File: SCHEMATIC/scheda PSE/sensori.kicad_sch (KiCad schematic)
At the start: 17 parts, among them J5 I2C_3V3, J6 UART0_3V3, Q3 IRLML9301, U7 SAM-M8Q, U8 MMA8451Q, U9 TC1047A

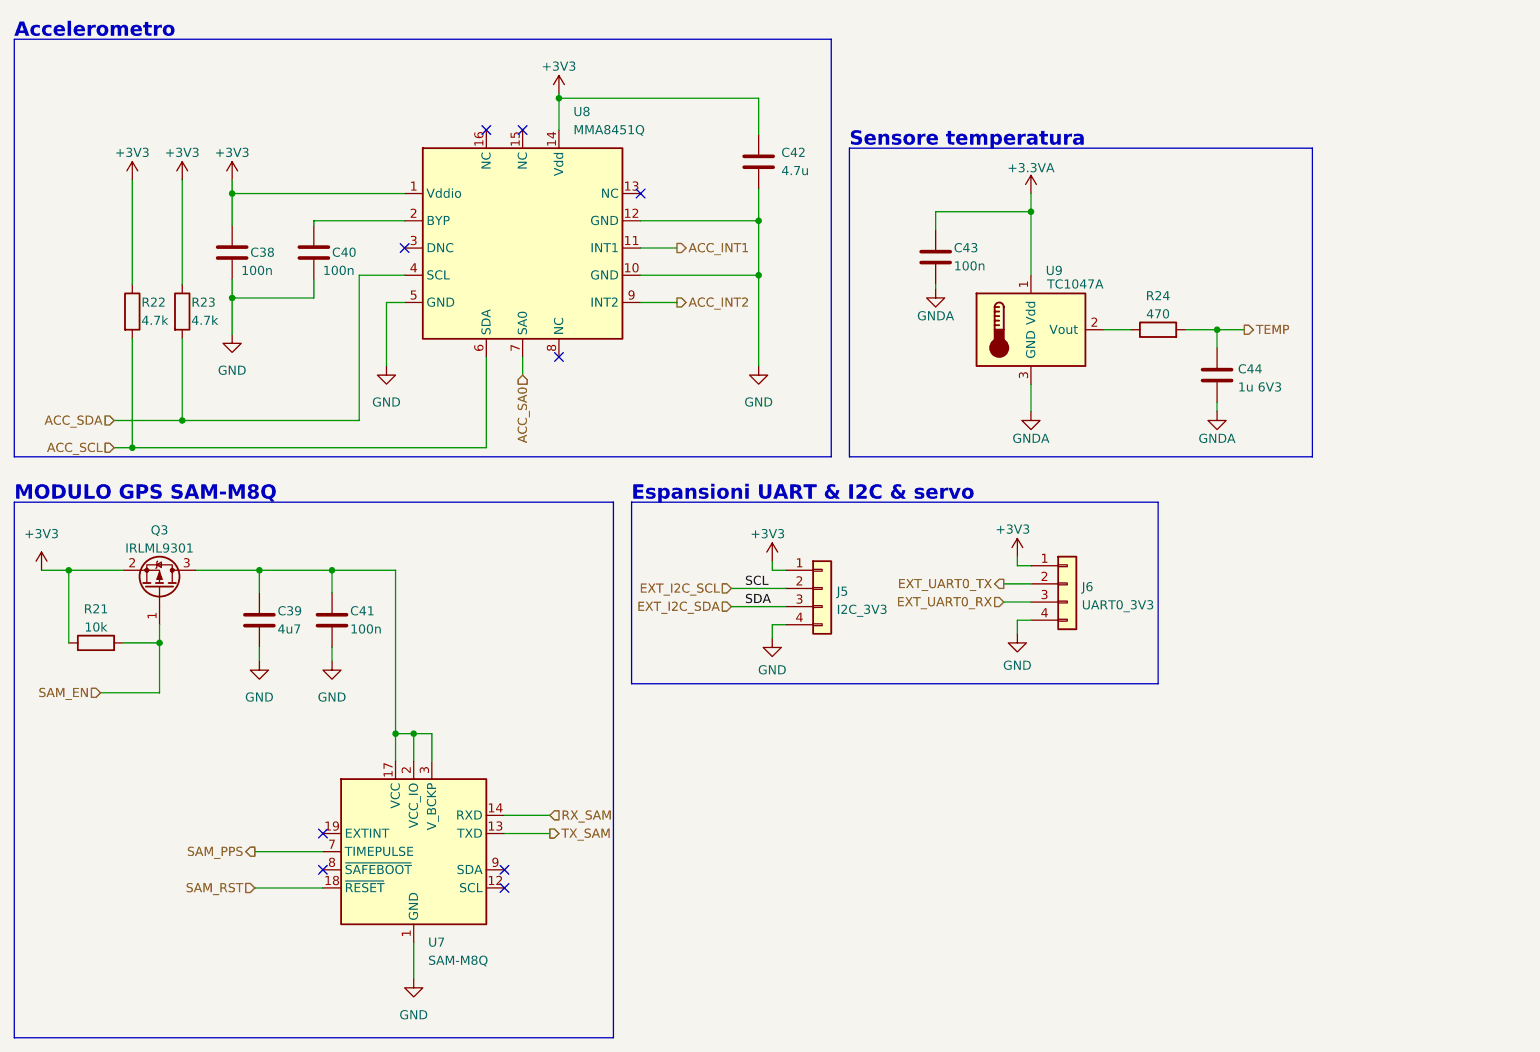
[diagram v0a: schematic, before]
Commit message: Aggiunte tutte le cose richieste dal prof
Aggiunte tutte le cose richieste dal prof:
wifi
servo
uscita led
MANCA DA METERE IL SOLDER MASK SUI PAD NON USATI DEL GPS
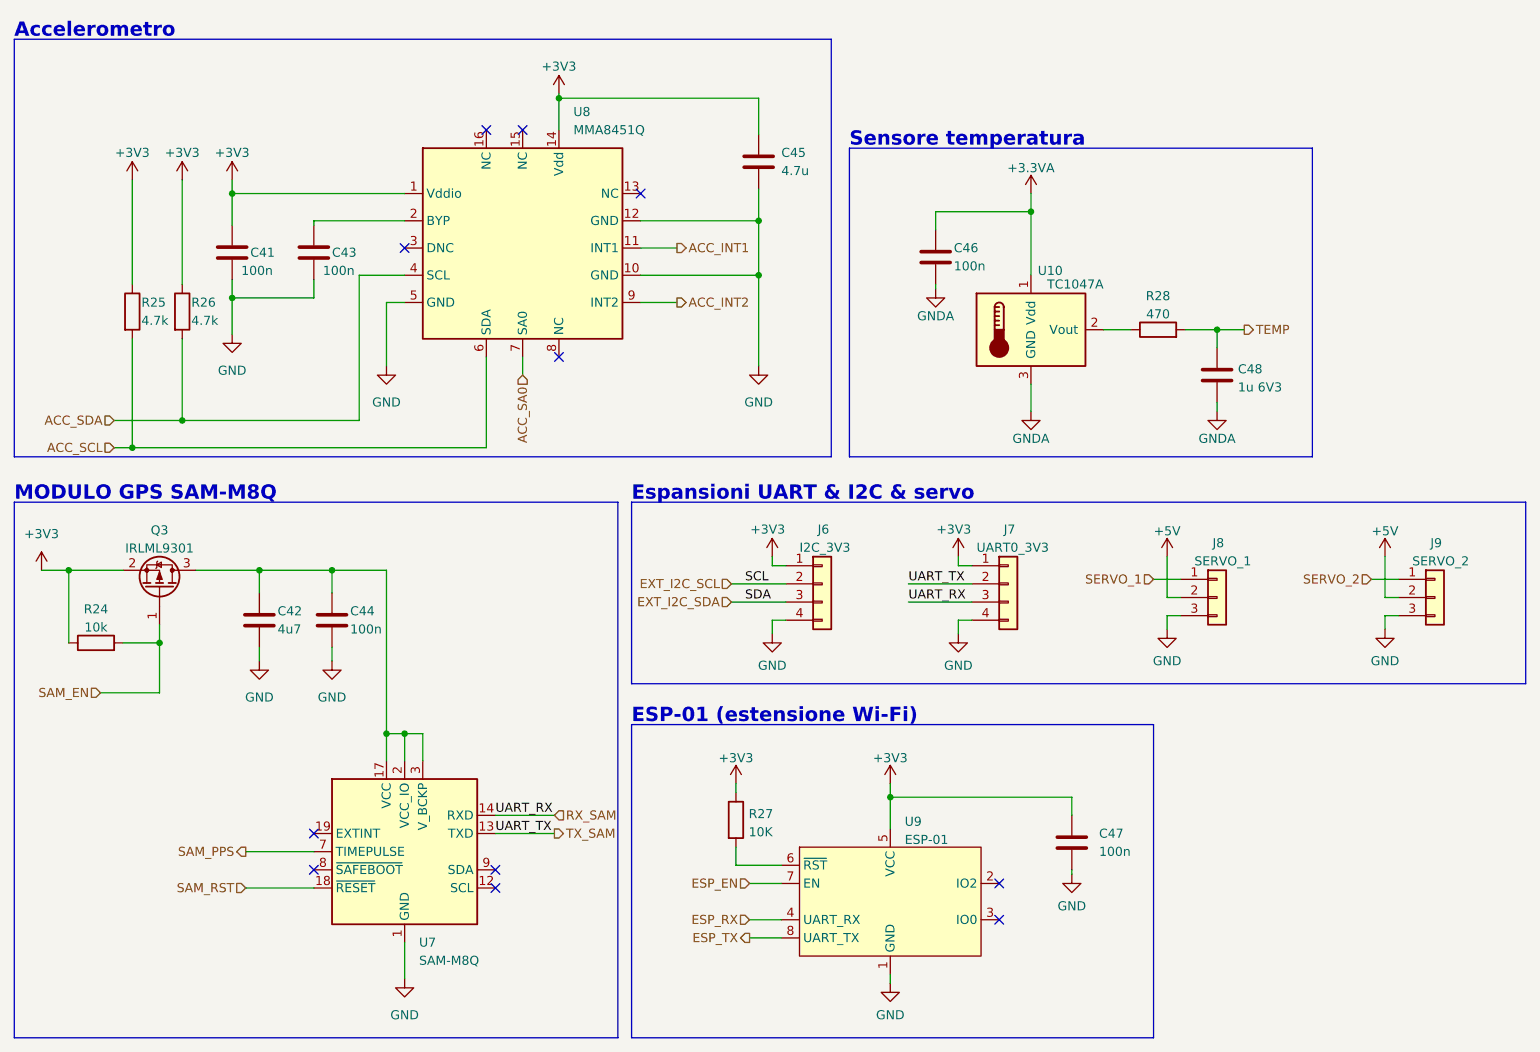
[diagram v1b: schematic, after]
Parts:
- added C47: 100n, Capacitor_SMD:C_0603_1608Metric, symbol Device:C
- added J8: SERVO_1, Connector_PinHeader_2.54mm:PinHeader_1x03_P2.54mm_Vertical, symbol Connector_Generic:Conn_01x03
- added J9: SERVO_2, Connector_PinHeader_2.54mm:PinHeader_1x03_P2.54mm_Vertical, symbol Connector_Generic:Conn_01x03
- added R27: 10K, Resistor_SMD:R_0603_1608Metric, symbol Device:R
- added U9: ESP-01, _PSE:ESP-01, symbol esp8266:ESP-01
- renumbered C38 to C41, C39 to C42, C40 to C43, C41 to C44, C42 to C45, C43 to C46, C44 to C48, J5 to J6, J6 to J7, R21 to R24, R22 to R25, R23 to R26, R24 to R28, U9 to U10
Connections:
- net EXT_UART0_RX is gone; now on net RX_SAM: J7.3 (Pin_3)
- net EXT_UART0_TX is gone; now on net TX_SAM: J7.2 (Pin_2)
- net +3V3: now also C47.1, R27.1, U9.5 (VCC)
- net GND: now also C47.2, J8.3 (Pin_3), J9.3 (Pin_3), U9.1 (GND)
- new net: R27.2, U9.6 (~{RST})
- new net +5V: J8.2 (Pin_2), J9.2 (Pin_2)
- new net ESP_EN: U9.7 (EN)
- new net ESP_RX: U9.4 (UART_RX)
- new net ESP_TX: U9.8 (UART_TX)
- new net SERVO_1: J8.1 (Pin_1)
- new net SERVO_2: J9.1 (Pin_1)
- no-connect marks 9 -> 11
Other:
- note added: "ESP-01 (estensione Wi-Fi)"
- moved on the sheet: J6, J7, U7

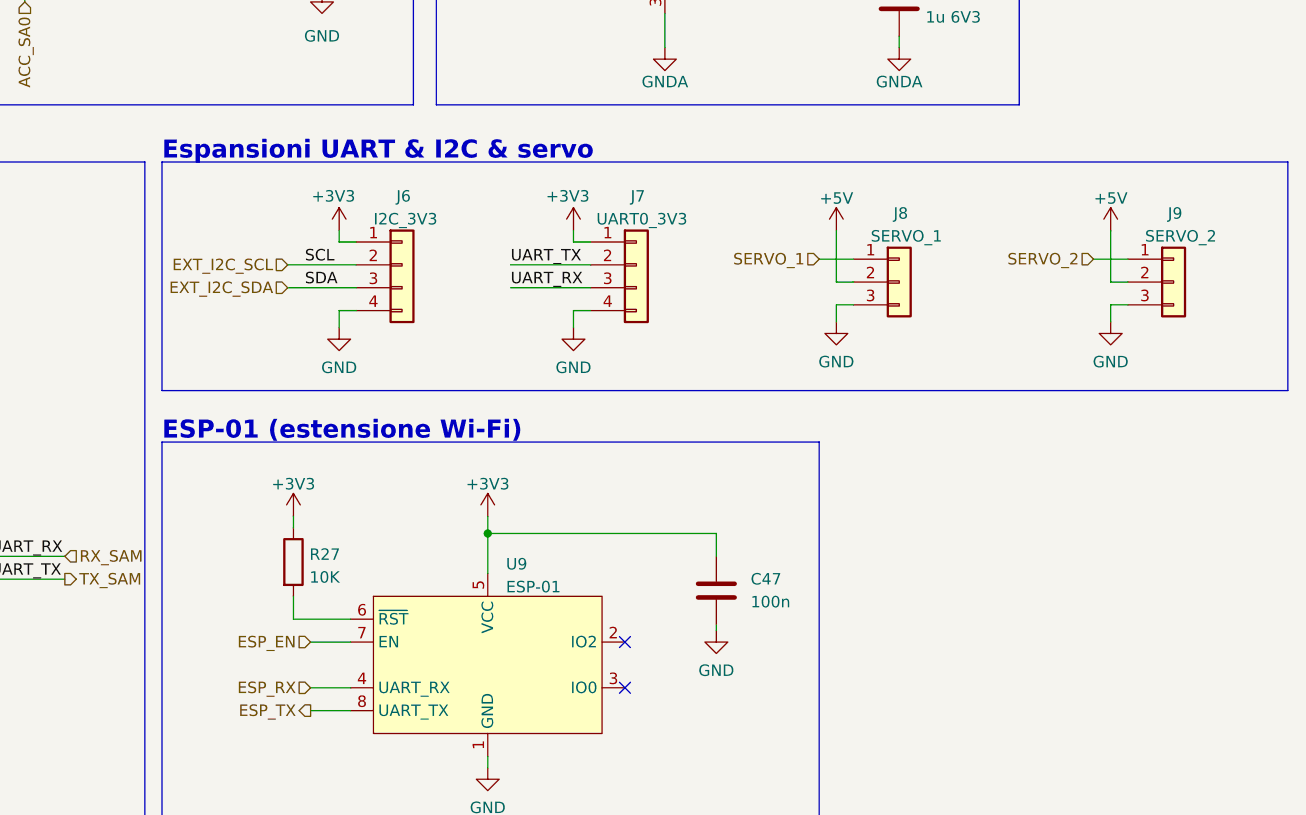
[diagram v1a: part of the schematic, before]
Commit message: Sistemate un po'di cose
aggiuno fori display e terzo servo e sistemate le serigrafie
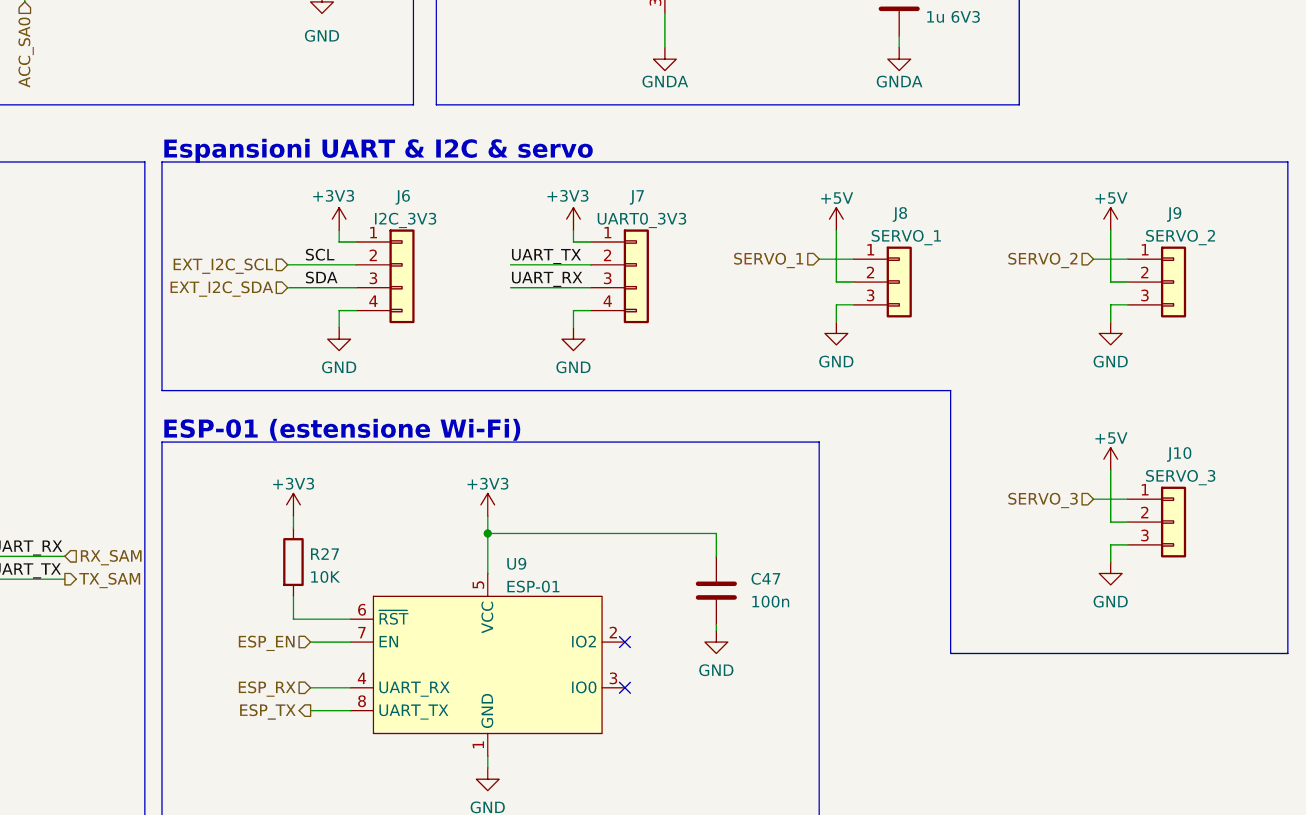
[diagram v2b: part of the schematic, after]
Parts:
- added J10: SERVO_3, Connector_PinHeader_2.54mm:PinHeader_1x03_P2.54mm_Vertical, symbol Connector_Generic:Conn_01x03
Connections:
- net +5V: now also J10.2 (Pin_2)
- net GND: now also J10.3 (Pin_3)
- new net SERVO_3: J10.1 (Pin_1)
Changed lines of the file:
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@@
+    (stroke (width 0) (type default) (color 0 0 0 0))
+  )
+  (polyline (pts (xy 273.05 140.97) (xy 273.05 86.36))
     (stroke (width 0) (type default) (color 0 0 0 0))
   )
@@
     (stroke (width 0) (type default) (color 0 0 0 0))
   )
+  (wire (pts (xy 253.365 126.365) (xy 255.27 126.365))
+    (stroke (width 0) (type default) (color 0 0 0 0))
+  )
   (wire (pts (xy 132.715 66.04) (xy 132.715 68.58))
     (stroke (width 0) (type default) (color 0 0 0 0))
@@
     (stroke (width 0) (type default) (color 0 0 0 0))
   )
+  (wire (pts (xy 253.365 120.65) (xy 253.365 126.365))
+    (stroke (width 0) (type default) (color 0 0 0 0))
+  )
   (wire (pts (xy 149.225 50.8) (xy 154.305 50.8))
     (stroke (width 0) (type default) (color 0 0 0 0))
@@
     (stroke (width 0) (type default) (color 0 0 0 0))
   )
-  (polyline (pts (xy 147.955 111.76) (xy 273.05 111.76))
+  (polyline (pts (xy 147.955 111.76) (xy 235.585 111.76))
     (stroke (width 0) (type default) (color 0 0 0 0))
   )
@@
     (stroke (width 0) (type default) (color 0 0 0 0))
   )
+  (wire (pts (xy 251.46 123.825) (xy 255.27 123.825))
+    (stroke (width 0) (type default) (color 0 0 0 0))
+  )
   (wire (pts (xy 85.09 63.5) (xy 85.09 74.93))
     (stroke (width 0) (type default) (color 0 0 0 0))
@@
     (stroke (width 0) (type default) (color 0 0 0 0))
   )
+  (polyline (pts (xy 235.585 111.76) (xy 235.585 140.97))
+    (stroke (width 0) (type default) (color 0 0 0 0))
+  )
   (wire (pts (xy 106.045 95.885) (xy 113.665 95.885))
     (stroke (width 0) (type default) (color 0 0 0 0))
@@
     (stroke (width 0) (type default) (color 0 0 0 0))
   )
+  (polyline (pts (xy 235.585 140.97) (xy 273.05 140.97))
+    (stroke (width 0) (type default) (color 0 0 0 0))
+  )
   (polyline (pts (xy 61.595 86.36) (xy 146.05 86.36))
     (stroke (width 0) (type default) (color 0 0 0 0))
@@
     (stroke (width 0) (type default) (color 0 0 0 0))
   )
+  (wire (pts (xy 253.365 130.81) (xy 253.365 128.905))
+    (stroke (width 0) (type default) (color 0 0 0 0))
+  )
   (polyline (pts (xy 220.98 117.475) (xy 147.955 117.475))
     (stroke (width 0) (type default) (color 0 0 0 0))
@@
     (stroke (width 0) (type default) (color 0 0 0 0))
   )
+  (wire (pts (xy 253.365 128.905) (xy 255.27 128.905))
+    (stroke (width 0) (type default) (color 0 0 0 0))
+  )
   (wire (pts (xy 162.56 134.62) (xy 162.56 137.16))
     (stroke (width 0) (type default) (color 0 0 0 0))
@@
   )
   (polyline (pts (xy 273.05 86.36) (xy 147.955 86.36))
-    (stroke (width 0) (type default) (color 0 0 0 0))
-  )
-  (polyline (pts (xy 273.05 111.76) (xy 273.05 86.36))
     (stroke (width 0) (type default) (color 0 0 0 0))
   )
@@
   (label "SCL" (at 163.83 97.79 0)
     (effects (font (size 1.27 1.27)) (justify left bottom))
+  )
+  (hierarchical_label "SERVO_3" (shape input) (at 251.46 123.825 180)
+    (effects (font (size 1.27 1.27)) (justify right))
   )
   (hierarchical_label "ACC_SDA" (shape input) (at 75.565 74.93 180)
@@
     (pin "2")
   )
+  (symbol (lib_id "Connector_Generic:Conn_01x03") (at 260.35 126.365 0) (unit 1)
+    (in_bom yes) (on_board yes)
+    (property "Reference" "J10" (id 0) (at 259.715 118.745 0)
+      (effects (font (size 1.27 1.27)) (justify left))
+    )
+    (property "Value" "SERVO_3" (id 1) (at 257.175 121.285 0)
+      (effects (font (size 1.27 1.27)) (justify left))
+    )
+    (property "Footprint" "Connector_PinHeader_2.54mm:PinHeader_1x03_P2.54mm_Vertical" (id 2) (at 260.35 126.365 0)
+      (effects (font (size 1.27 1.27)) hide)
+    )
+    (property "Datasheet" "~" (id 3) (at 260.35 126.365 0)
+      (effects (font (size 1.27 1.27)) hide)
+    )
+    (pin "1")
+    (pin "2")
+    (pin "3")
+  )
+  (symbol (lib_id "power:+5V") (at 253.365 120.65 0) (unit 1)
+    (in_bom yes) (on_board yes) (fields_autoplaced)
+    (property "Reference" "#PWR0104" (id 0) (at 253.365 124.46 0)
+      (effects (font (size 1.27 1.27)) hide)
+    )
+    (property "Value" "+5V" (id 1) (at 253.365 117.0742 0))
+    (property "Footprint" "" (id 2) (at 253.365 120.65 0)
+      (effects (font (size 1.27 1.27)) hide)
+    )
+    (property "Datasheet" "" (id 3) (at 253.365 120.65 0)
+      (effects (font (size 1.27 1.27)) hide)
+    )
+    (pin "1")
+  )
   (symbol (lib_id "Device:C") (at 229.87 68.58 0) (unit 1)
     (in_bom yes) (on_board yes) (fields_autoplaced)
@@
       (effects (font (size 1.27 1.27)) hide)
     )
+    (pin "1")
+  )
+  (symbol (lib_id "power:GND") (at 253.365 130.81 0) (unit 1)
+    (in_bom yes) (on_board yes) (fields_autoplaced)
+    (property "Reference" "#PWR0105" (id 0) (at 253.365 137.16 0)
+      (effects (font (size 1.27 1.27)) hide)
+    )
+    (property "Value" "GND" (id 1) (at 253.365 135.2534 0))
+    (property "Footprint" "" (id 2) (at 253.365 130.81 0)
+      (effects (font (size 1.27 1.27)) hide)
+    )
+    (property "Datasheet" "" (id 3) (at 253.365 130.81 0)
+      (effects (font (size 1.27 1.27)) hide)
+    )

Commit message: Versione definitiva inviata ai prof
Sistemato tutto e inviato il tutto ai prof
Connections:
- net ACC_SA0 is gone; now on net GND: U8.7 (SA0)
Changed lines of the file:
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@@
     (stroke (width 0) (type default) (color 0 0 0 0))
   )
-  (wire (pts (xy 132.715 66.04) (xy 132.715 68.58))
+  (wire (pts (xy 132.715 66.04) (xy 132.715 67.31))
     (stroke (width 0) (type default) (color 0 0 0 0))
   )
@@
     (effects (font (size 2 2) (thickness 0.4) bold) (justify left bottom))
   )
-  (label "UART_RX" (at 128.905 130.175 0)
+  (label "UART_TX" (at 128.905 130.175 0)
     (effects (font (size 1.27 1.27)) (justify left bottom))
   )
-  (label "UART_TX" (at 186.69 97.79 0)
+  (label "UART_TX" (at 186.69 100.33 0)
     (effects (font (size 1.27 1.27)) (justify left bottom))
   )
@@
     (effects (font (size 1.27 1.27)) (justify left bottom))
   )
-  (label "UART_TX" (at 128.905 132.715 0)
+  (label "UART_RX" (at 128.905 132.715 0)
     (effects (font (size 1.27 1.27)) (justify left bottom))
   )
-  (label "UART_RX" (at 186.69 100.33 0)
+  (label "UART_RX" (at 186.69 97.79 0)
     (effects (font (size 1.27 1.27)) (justify left bottom))
   )
@@
   )
   (hierarchical_label "SERVO_2" (shape input) (at 251.46 97.155 180)
-    (effects (font (size 1.27 1.27)) (justify right))
-  )
-  (hierarchical_label "ACC_SA0" (shape input) (at 132.715 68.58 270)
     (effects (font (size 1.27 1.27)) (justify right))
   )
@@
     (pin "9")
   )
+  (symbol (lib_id "power:GND") (at 132.715 67.31 0) (unit 1)
+    (in_bom yes) (on_board yes) (fields_autoplaced)
+    (property "Reference" "#PWR0107" (id 0) (at 132.715 73.66 0)
+      (effects (font (size 1.27 1.27)) hide)
+    )
+    (property "Value" "GND" (id 1) (at 132.715 72.39 0))
+    (property "Footprint" "" (id 2) (at 132.715 67.31 0)
+      (effects (font (size 1.27 1.27)) hide)
+    )
+    (property "Datasheet" "" (id 3) (at 132.715 67.31 0)
+      (effects (font (size 1.27 1.27)) hide)
+    )
+    (pin "1")
+  )
   (symbol (lib_id "power:+3V3") (at 78.105 41.275 0) (unit 1)
